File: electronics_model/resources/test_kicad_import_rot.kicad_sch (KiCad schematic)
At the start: 3 parts

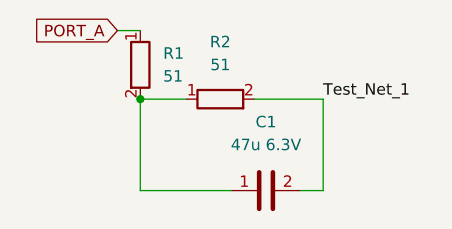
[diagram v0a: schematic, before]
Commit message: dedup symbols, name nodes
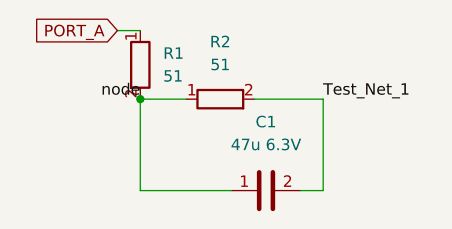
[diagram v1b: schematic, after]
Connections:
- net node: now reaches C1.1, R1.2, R2.1
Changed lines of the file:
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@@
     (stroke (width 0) (type default) (color 0 0 0 0))
+  )
+  (label "node" (at 91.44 86.36 180)
+    (effects (font (size 1.27 1.27)) (justify right bottom))
   )
   (label "Test_Net_1" (at 111.76 86.36 0)
@@
       (effects (font (size 1.27 1.27)) (justify right) hide)
     )
-  )
-  (symbol (lib_name "R_1") (lib_id "Device:R") (at 100.33 86.36 90) (unit 1)
-    (in_bom yes) (on_board yes) (fields_autoplaced)
-    (property "Reference" "R2" (id 0) (at 100.33 80.01 90))
-    (property "Value" "51" (id 1) (at 100.33 82.55 90))
-    (property "Footprint" "" (id 2) (at 100.33 88.138 90)
-      (effects (font (size 1.27 1.27)) hide)
-    )
-    (property "Datasheet" "~" (id 3) (at 100.33 86.36 0)
-      (effects (font (size 1.27 1.27)) hide)
-    )
-    (pin "1")
-    (pin "2")
   )
   (symbol (lib_id "Device:R") (at 91.44 82.55 0) (unit 1)
@@
     )
     (property "Datasheet" "~" (id 3) (at 91.44 82.55 0)
+      (effects (font (size 1.27 1.27)) hide)
+    )
+    (pin "1")
+    (pin "2")
+  )
+  (symbol (lib_id "Device:R") (at 100.33 86.36 90) (unit 1)
+    (in_bom yes) (on_board yes) (fields_autoplaced)
+    (property "Reference" "R2" (id 0) (at 100.33 80.01 90))
+    (property "Value" "51" (id 1) (at 100.33 82.55 90))
+    (property "Footprint" "" (id 2) (at 100.33 88.138 90)
+      (effects (font (size 1.27 1.27)) hide)
+    )
+    (property "Datasheet" "~" (id 3) (at 100.33 86.36 0)
       (effects (font (size 1.27 1.27)) hide)
     )
@@
       (reference "R1") (unit 1) (value "51") (footprint "")
     )
-    (path "/053518b3-994e-4e57-8f86-80f07be5a072"
+    (path "/de9fc76a-7e30-46c3-8ad1-aa14fd32a1bf"
       (reference "R2") (unit 1) (value "51") (footprint "")
     )

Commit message: unify naming
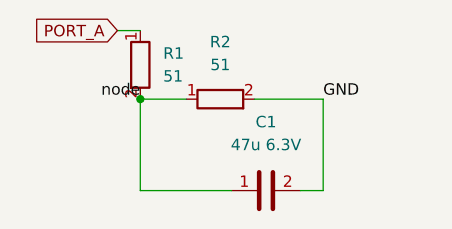
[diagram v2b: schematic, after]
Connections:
- net Test_Net_1 renamed GND
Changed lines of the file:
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@@
     (effects (font (size 1.27 1.27)) (justify right bottom))
   )
-  (label "Test_Net_1" (at 111.76 86.36 0)
+  (label "GND" (at 111.76 86.36 0)
     (effects (font (size 1.27 1.27)) (justify left bottom))
   )
